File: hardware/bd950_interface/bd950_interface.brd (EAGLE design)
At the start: 100 x 50 mm, 16 parts, among them IC1 FT4232HL, IC2 MAX208ECWG, IC3 4050D, X1 ECG.0B.304.CLV

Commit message: Continue work on BD950 interface board
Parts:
- added C1, C2, C3: 3.3uF, resistor:C0603
- added IC4: AT93C46A-10SQ-2.7, atmel:SOIC8
- added Q1: (no value), adafruit:HC49/S
- added R10: 2.2k, resistor:R0603
- added R11, R6: 12k, resistor:R0603
- added R7, R8, R9: 10k, resistor:R0603
- moved R5 150.1 mm to (77.0, 28.0)
- moved R4 142.8 mm to (78.0, 22.0)
- moved IC3 141.8 mm to (88.0, 25.0)
- moved IC2 93.9 mm to (27.0, 22.0), turned to 90 degrees
- moved IC1 3.00 mm to (52.0, 23.0)
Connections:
- removed net VCCIO: IC1.20, IC1.31, IC1.42, IC1.56
- removed net VCORE: IC1.12, IC1.37, IC1.64
- removed net VPHY: IC1.4
- removed net VPLL: IC1.9
- new net +3V3: IC1.20, IC1.31, IC1.4, IC1.42, IC1.50, IC1.56, IC1.9, IC4.8, R11.2, R7.2, R8.2, R9.2
- new net EECLK: IC1.62, IC4.2, R8.1
- new net EECS: IC1.63, IC4.1, R9.1
- new net EEDATA: IC1.61, IC4.3, R10.2
- new net N$10: C1.1, IC1.12, IC1.37, IC1.49, IC1.64
- new net N$11: C3.1, IC1.3, Q1.1
- new net N$12: C2.1, IC1.2, Q1.2
- new net N$13: IC1.14, R11.1
- new net N$6: IC1.6, R6.2
- new net N$9: IC4.4, R10.1, R7.1
- new net UART1_RXD: IC1.17, IC2.6
- new net UART1_TXD: IC1.16, IC2.5
- new net UART2_RXD: IC1.27, IC2.4
- new net UART2_TXD: IC1.26, IC2.18
- new net UART3_RXD: IC2.22
- new net UART3_TXD: IC1.38, IC1.39, IC2.19
- new net UART4_RXD: IC1.52, IC2.17, IC2.21
- new net UART4_TXD: IC1.48
- net 1PPS_PORT1: now also IC1.23
- net 1PPS_PORT2: now also IC1.33
- net 1PPS_PORT3: now also IC1.45
- net 1PPS_PORT4: now also IC1.58
- net GND: now also C1.2, C2.2, C3.2, IC1.13, IC4.5, R6.1
- net PORT1_RXD: now also IC2.2
- net PORT2_RXD: now also IC2.1
- net PORT3_RXD: now also IC2.24
- net PORT4_RXD: now also IC2.20
- net PORT4_TXD: now also IC2.16, IC2.23, IC2.3, IC2.7
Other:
- board size 100 x 50 mm -> 100 x 34 mm

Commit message: Make BD950 interface board USB powered
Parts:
- removed D7: BAT60J, diode:SOD323_ST
- added C10, C6, C8, C9: 0.1uF, resistor:C0603
- added C4, C5: 10uF, resistor:C0603
- added IC5: 786TV, linear:TO220V
- added R12: 1k, resistor:R0603
- added R13: 4.7k, resistor:R0603
- added U$1: MUSBB15130, adafruit:MUSBB15130
- R11: value 12k -> 10k
- moved IC1 3.00 mm to (52.0, 20.0), turned to 180 degrees
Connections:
- removed net V+: C7.1, D7.C, U$2.A2, U$2.B2
- removed net VCC: IC2.9
- removed net VSS: IC3.8
- new net N$14: C6.1, IC2.10
- new net N$15: IC1.14, R12.2
- new net N$16: C6.2, IC2.12
- new net N$17: C8.1, IC2.13
- new net N$18: C8.2, IC2.14
- new net N$19: C9.1, IC2.15
- new net N$20: C10.1, IC2.11
- new net USB_D+: IC1.8, U$1.3
- new net USB_D-: IC1.7, U$1.2
- net +3V3: now also C10.2, C4.1, IC2.9, IC3.1, IC5.3; no longer R11.2
- net GND: now also C4.2, C5.2, C9.2, IC3.8, IC5.2, R11.2, U$1.5, X1.4
- net N$13: now also R12.1, R13.2; no longer IC1.14
- net N$2: now also C5.1, IC5.1; no longer D7.A
- net VDD: now also C7.1, R13.1, U$1.1, U$2.A2, U$2.B2; no longer IC3.1

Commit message: Continue laying out BD950 interface board
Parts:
- removed R11: 10k, resistor:R0603
- removed R13: 4.7k, resistor:R0603
- C2, C3: value 3.3uF -> 27pF
- LED1, LED2, LED3: device adafruit:LED5MM -> adafruit:CHIP-LED0603
- moved IC5 131.6 mm to (24.0, 19.6), turned to 90 degrees
- moved R1 120.6 mm to (110.2, 19.2)
- moved IC4 117.2 mm to (78.2, 29.2), turned to 270 degrees
- moved R3 72.0 mm to (3.96, 29.7), turned to 180 degrees
- moved R2 63.6 mm to (15.2, 29.6), turned to 180 degrees
- moved C7 56.9 mm to (71.2, 36.3)
- moved LED2 34.3 mm to (3.93, 31.9), turned to 90 degrees
- moved U$1 24.3 mm to (26.7, 30.2)
- moved Q1 21.3 mm to (60.9, 30.6), turned to 0 degrees
- moved LED1 17.7 mm to (15.3, 31.9), turned to 90 degrees
- moved LED3 16.7 mm to (9.44, 31.9), turned to 90 degrees
- moved R5 16.5 mm to (83.4, 12.8)
- moved X1 14.9 mm to (89.6, 25.4)
- moved R19 14.7 mm to (9.45, 29.6)
- moved IC2 13.1 mm to (40.1, 20.8), turned to 270 degrees
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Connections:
- removed net N$13: R11.1, R12.1, R13.2
- net +3V3: now also R12.1
- net GND: now also LED1.C, LED2.C, LED3.C; no longer LED1.K, LED2.K, LED3.K, R11.2
- net PORT1_TXD: now also IC2.7
- net PORT2_TXD: now also IC2.3
- net PORT3_TXD: now also IC2.23
- net PORT4_TXD: no longer IC2.23, IC2.3, IC2.7
- net VDD: no longer R13.1
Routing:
- net LED_CMR_RX: track 0.00 -> 48.4 mm
- net LED_TRACKING: track 0.00 -> 43.0 mm
- net LED_POWER: track 0.00 -> 35.8 mm
- net PORT2_RXD: track 0.00 -> 33.4 mm
- net PORT2_TXD: track 0.00 -> 31.9 mm
- net N$8: track 0.00 -> 31.5 mm
- net PORT3_RXD: track 0.00 -> 26.3 mm
- net PORT3_TXD: track 0.00 -> 24.5 mm
- net PORT1_RXD: track 0.00 -> 24.3 mm
- net PORT4_RXD: track 0.00 -> 20.3 mm
- net PORT1_TXD: track 0.00 -> 17.9 mm
- net 1PPS: track 0.00 -> 16.2 mm
- net PORT4_TXD: track 0.00 -> 16.2 mm
- net EECS: track 0.00 -> 14.5 mm
- net EECLK: track 0.00 -> 14.2 mm
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
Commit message: Finish laying out BD950 interface board
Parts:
- C4, C5: device resistor:C0603 -> resistor:C0805
- moved C9 190.6 mm to (50.3, 14.5), turned to 270 degrees
- moved C10 190.3 mm to (29.6, 15.0), turned to 90 degrees
- moved C8 185.2 mm to (48.2, 14.5), turned to 90 degrees
- moved C6 176.2 mm to (31.6, 15.0), turned to 270 degrees
- moved R12 170.7 mm to (52.4, 25.7)
- moved C4 152.1 mm to (22.1, 26.4)
- moved C5 148.1 mm to (26.3, 16.3), turned to 270 degrees
- moved C2 145.4 mm to (68.7, 30.6), turned to 90 degrees
- moved C3 141.8 mm to (52.9, 30.6), turned to 90 degrees
- moved R9 137.9 mm to (84.7, 30.3), turned to 90 degrees
- moved R8 136.2 mm to (87.1, 30.3), turned to 90 degrees
- moved R7 134.7 mm to (89.6, 30.3), turned to 90 degrees
- moved R10 130.2 mm to (72.3, 26.4), turned to 270 degrees
- moved R6 101.9 mm to (67.8, 26.3), turned to 180 degrees
- moved C1 100.3 mm to (70.3, 17.5), turned to 90 degrees
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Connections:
- removed net N$2: C5.1, IC5.1
- net UART3_RXD: now also IC1.39
- net UART3_TXD: no longer IC1.39
- net UART4_RXD: no longer IC2.21
- net UART4_TXD: now also IC2.21
- net VDD: now also C5.1, IC5.1
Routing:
- net +3V3: track 0.00 -> 167.5 mm, vias 0 -> 4
- net VDD: track 0.00 -> 42.1 mm
- net USB_D-: track 0.00 -> 38.9 mm
- net USB_D+: track 0.00 -> 37.6 mm
- net UART4_RXD: track 0.00 -> 35.4 mm, vias 0 -> 2
- net UART4_TXD: track 0.00 -> 32.2 mm, vias 0 -> 2
- net N$10: track 0.00 -> 31.9 mm, vias 0 -> 4
- net UART3_RXD: track 0.00 -> 26.6 mm, vias 0 -> 2
- net 1PPS_PORT2: track 0.00 -> 24.7 mm
- net UART3_TXD: track 0.00 -> 24.3 mm, vias 0 -> 2
- net UART1_TXD: track 0.00 -> 24.2 mm, vias 0 -> 2
- net UART1_RXD: track 0.00 -> 23.8 mm, vias 0 -> 2
- net UART2_RXD: track 0.00 -> 22.1 mm, vias 0 -> 2
- net 1PPS_PORT1: track 0.00 -> 21.1 mm, vias 0 -> 2
- net 1PPS_PORT4: track 0.00 -> 20.5 mm, vias 0 -> 2
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
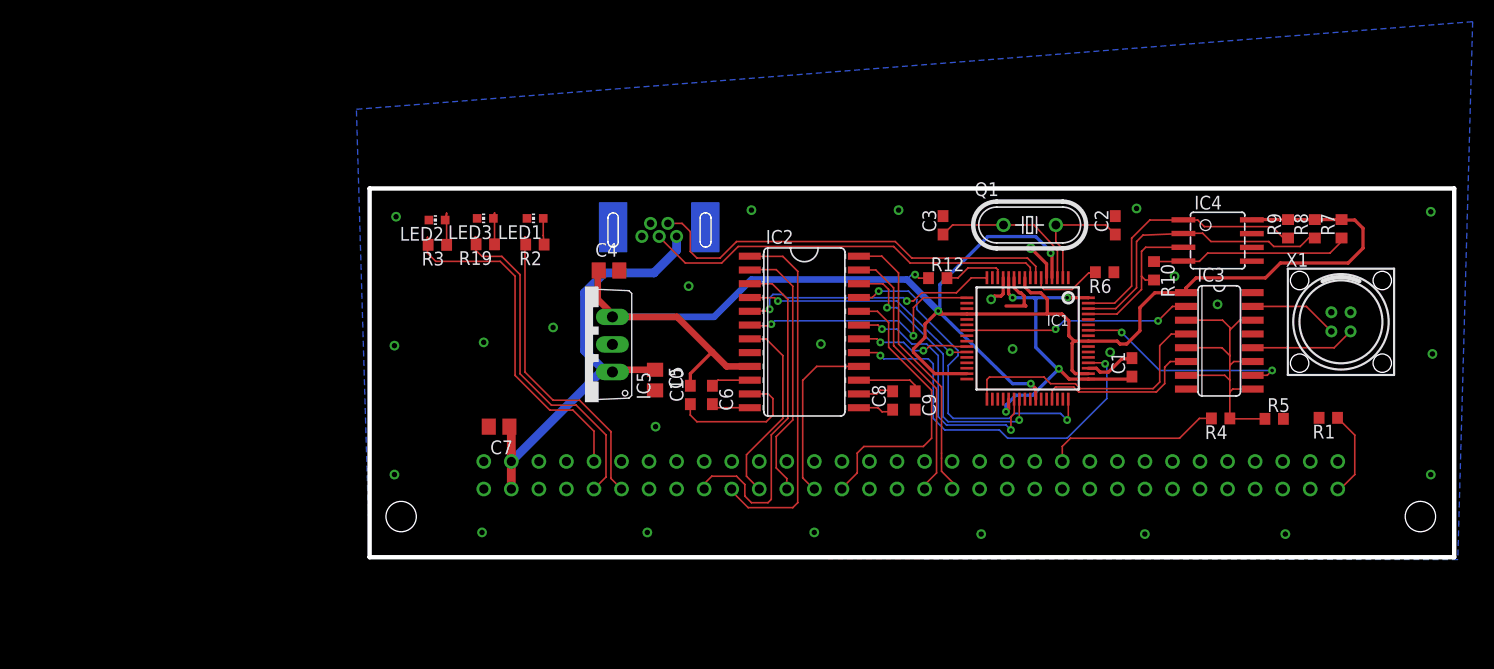
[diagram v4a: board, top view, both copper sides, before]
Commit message: WIP Fix BD950 interface board layout issues
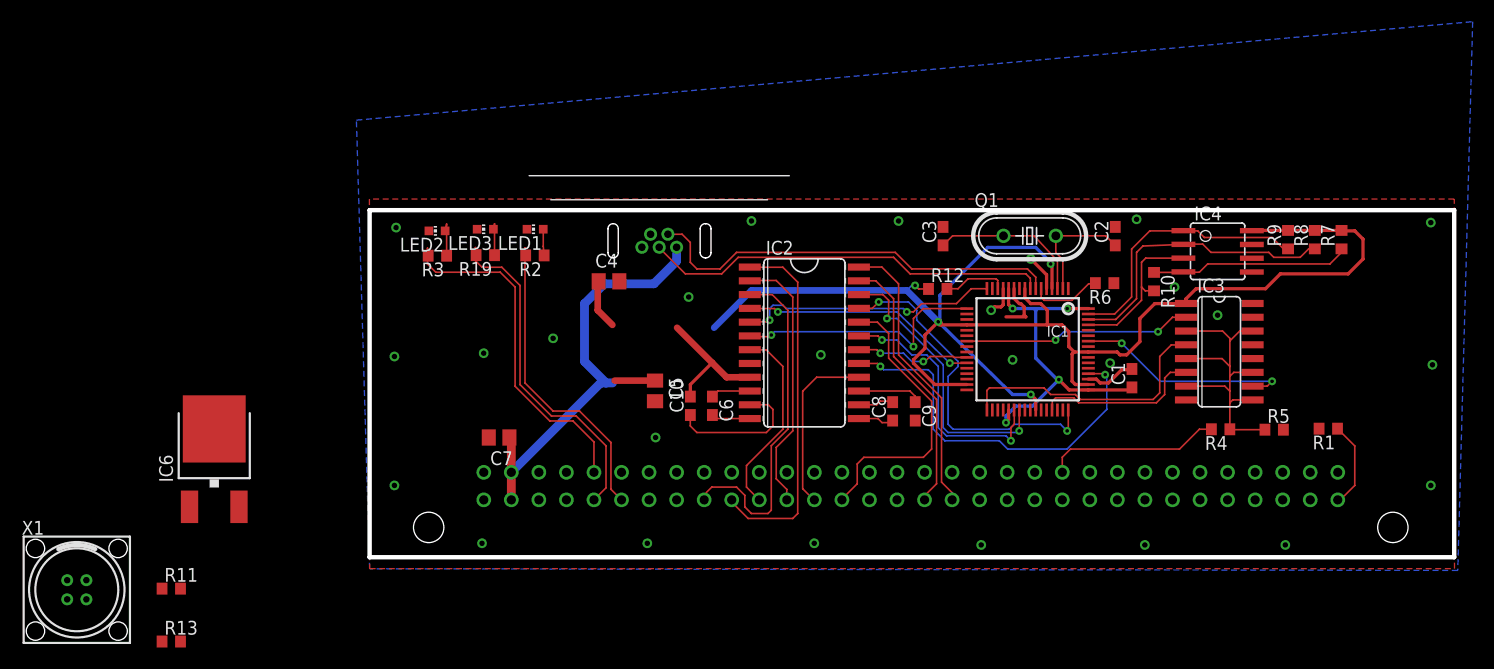
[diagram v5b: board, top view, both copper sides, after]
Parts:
- removed IC5: 786TV, linear:TO220V
- added IC6: LM317MDT, v-reg:DPACK
- added R11: 383, resistor:R0603
- added R13: 649, resistor:R0603
- U$2: value PCN13-64S-2.54DS(71) -> 294721
- moved X1 119.1 mm to (-27.0, -3.00)
- moved C1 1.00 mm to (70.3, 16.5)
- moved C10 1.00 mm to (29.6, 14.0)
- moved C2 1.00 mm to (68.7, 29.6)
- moved C3 1.00 mm to (52.9, 29.6)
- moved C4 1.00 mm to (22.1, 25.4)
- moved C5 1.00 mm to (26.3, 15.3)
- moved C6 1.00 mm to (31.6, 14.0)
- moved C7 1.00 mm to (11.9, 11.0)
- moved C8 1.00 mm to (48.2, 13.5)
- moved C9 1.00 mm to (50.3, 13.5)
- moved IC1 1.00 mm to (60.7, 19.2)
- moved IC2 1.00 mm to (40.1, 19.8)
- moved IC3 1.00 mm to (78.3, 18.9)
- moved IC4 1.00 mm to (78.2, 28.2)
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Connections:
- new net N$2: IC6.1, R11.2, R13.2
- net +3V3: now also IC6.4, R13.1; no longer IC5.3
- net GND: now also R11.1; no longer IC5.2
- net VDD: now also IC6.3; no longer IC5.1
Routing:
- net +3V3: track 167.5 -> 151.9 mm
- net 1PPS_EXT0: track 9.65 -> 0.00 mm
- net 1PPS_EXT1: track 8.22 -> 0.00 mm
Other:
- board size 100 x 34 mm -> 100 x 32 mm

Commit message: Rev 2 of BD950 interface board
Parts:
- removed X1: ECG.0B.304.CLV, con-lemo:EZG-0B-0K-304
- added C11: 0.1uF, resistor:C0603
- added R14: 10k, rcl:R0603
- added U$3: ECG.0B.304.CLV, adafruit:ECG.0B.CLV
- added U$4: SN74LVC1G123, adafruit:DCU_(R-PDSO-G8)
- moved R13 49.4 mm to (25.8, 14.6), turned to 270 degrees
- moved R11 43.7 mm to (21.9, 14.2)
- moved IC6 33.1 mm to (17.2, 19.3), turned to 90 degrees
- moved R6 17.8 mm to (50.4, 29.4), turned to 270 degrees
- moved R5 12.0 mm to (71.4, 11.0)
- moved R4 11.0 mm to (67.5, 11.0)
- moved LED1 10.5 mm to (5.00, 28.1)
- moved LED3 10.0 mm to (5.00, 22.0)
- moved C4 9.22 mm to (27.4, 17.9)
- moved R2 6.87 mm to (8.37, 28.0), turned to 0 degrees
- moved C5 6.49 mm to (27.3, 21.7), turned to 0 degrees
- moved R19 6.06 mm to (8.37, 22.2), turned to 0 degrees
- moved LED2 5.28 mm to (5.00, 25.0)
- moved U$1 5.00 mm to (22.7, 26.2)
- moved R3 3.41 mm to (8.39, 25.1), turned to 0 degrees
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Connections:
- new net N$13: R4.1, R5.1, U$4.2
- new net N$21: C11.2, U$4.6
- new net N$23: C11.1, R14.2, U$4.7
- net +3V3: now also R14.1, U$4.3, U$4.8
- net 1PPS_EXT0: now also U$3.P$4; no longer X1.3
- net 1PPS_EXT1: now also U$3.P$3; no longer X1.2
- net GND: now also U$3.P$1, U$3.P$2, U$4.1, U$4.4; no longer X1.1, X1.4
- net N$8: now also U$4.5; no longer R4.1, R5.1
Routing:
- net +3V3: track 151.9 -> 177.3 mm
- net N$13: track 0.00 -> 12.5 mm
- net 1PPS_EXT0: track 0.00 -> 11.4 mm
- net 1PPS: track 16.2 -> 5.25 mm
- net 1PPS_EXT1: track 0.00 -> 10.6 mm
- net VDD: track 41.8 -> 33.8 mm, vias 0 -> 1
- net N$6: track 6.59 -> 14.2 mm
- net LED_POWER: track 32.5 -> 25.1 mm
- net LED_TRACKING: track 31.8 -> 24.6 mm
- net USB_D+: track 37.6 -> 44.3 mm
- net N$23: track 0.00 -> 6.44 mm
- net USB_D-: track 38.9 -> 45.3 mm
- net N$2: track 0.00 -> 6.26 mm
- net N$21: track 0.00 -> 2.91 mm
- net LED_CMR_RX: track 29.1 -> 31.7 mm
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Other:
- outline, holes or cut-outs redrawn
